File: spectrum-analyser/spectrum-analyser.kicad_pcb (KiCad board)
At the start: 2 copper layers, 50 x 95 mm, 41 parts, among them J1 Conn_Coaxial, J2 Conn_01x02, Q1 PMOS, Q2 PMOS, Q3 Q_PMOS_GSD, Q4 Q_NMOS_GSD, Q5 Q_NMOS_GSD, SW1 SW_SPDT, SW2 SW_UP, SW3 SW_RIGHT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

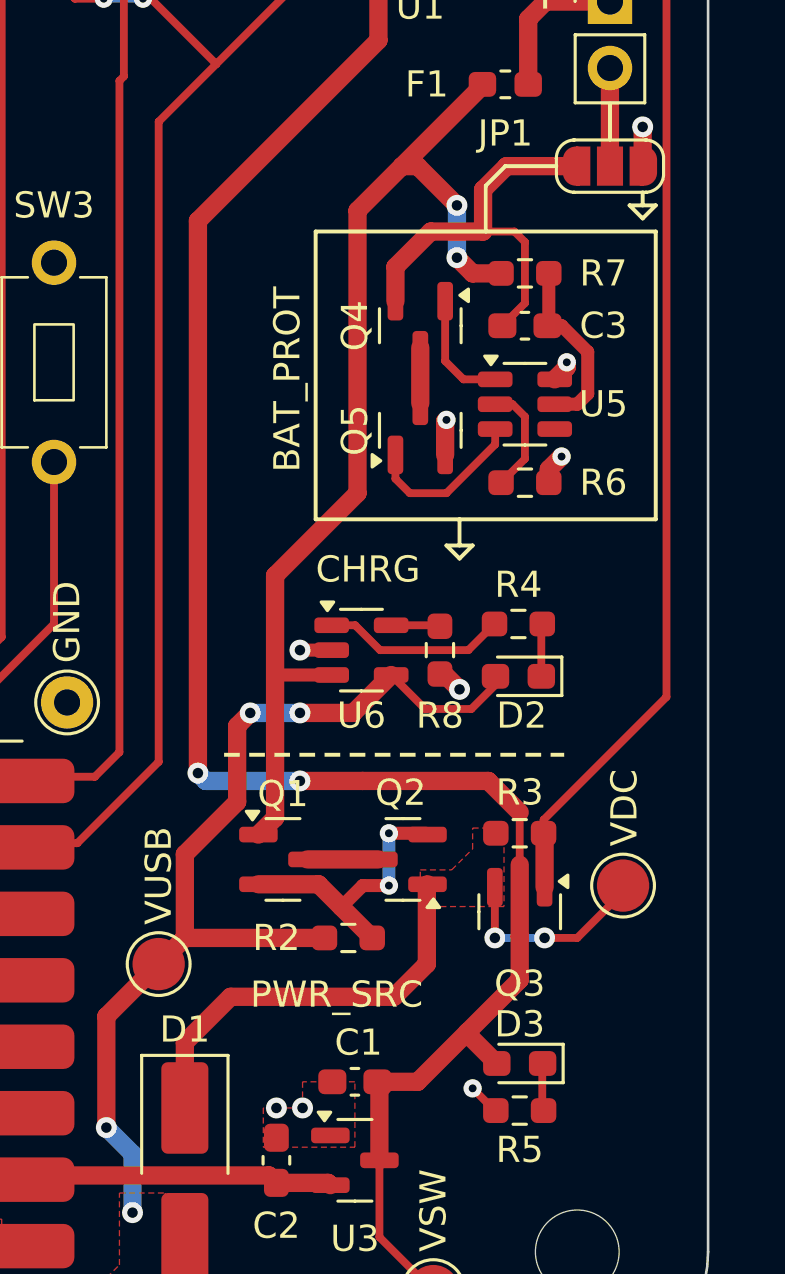
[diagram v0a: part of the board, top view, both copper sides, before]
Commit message: Assign component values and add charger capacitors
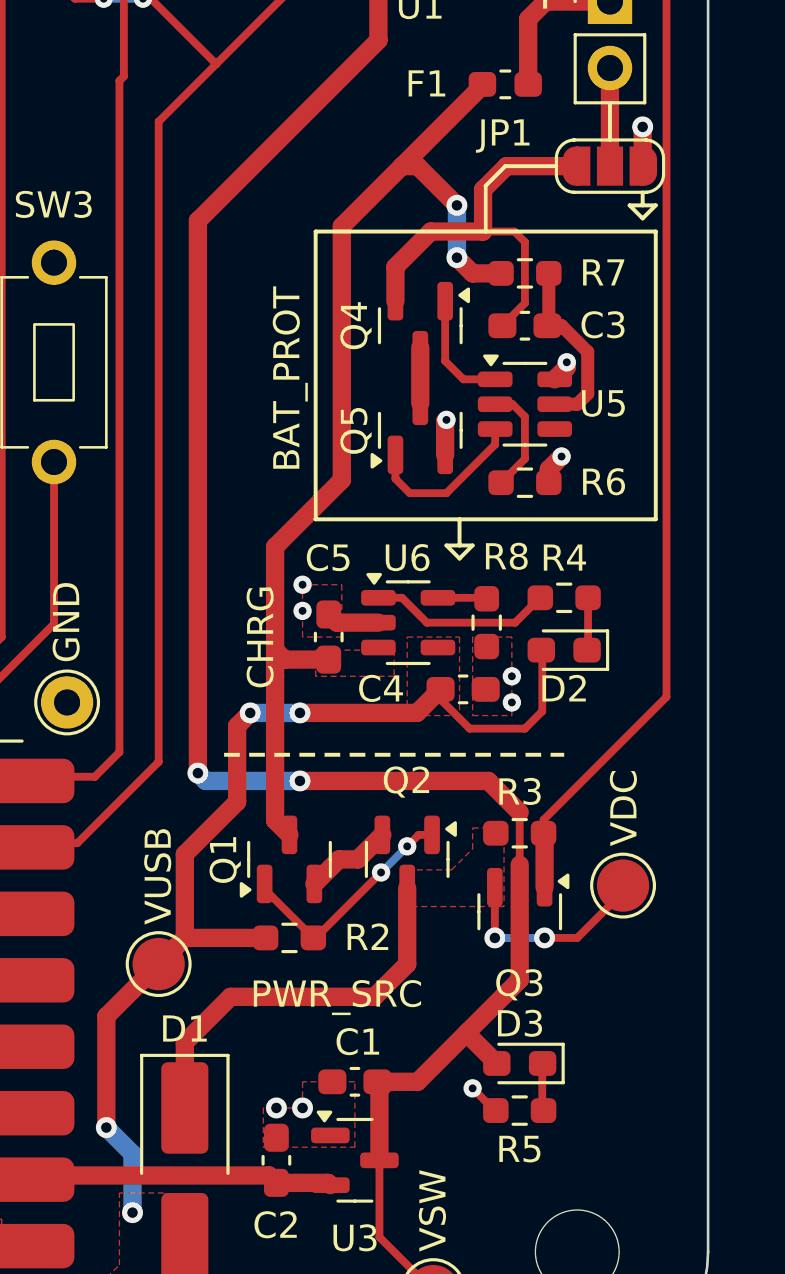
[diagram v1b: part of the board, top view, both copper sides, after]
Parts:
- added C4: 4u7, Capacitor_SMD:C_0603_1608Metric_Pad1.08x0.95mm_HandSolder, F.Cu at (135.6, 128.5)
- added C5: 4u7, Capacitor_SMD:C_0603_1608Metric_Pad1.08x0.95mm_HandSolder, F.Cu at (130.5, 126.5)
- C1, C2: value C -> 1u
- F1: value Fuse -> 3A
- J1: value Conn_Coaxial -> SMA
- Q1, Q2: value PMOS -> Q_PMOS_GSD
- R1, R2: value R -> 10k
- R8: value 12k -> 10k
- moved R2 2.25 mm to (129.0, 138.0)
- moved R8 2.07 mm to (136.5, 126.0)
- moved U6 2.07 mm to (133.5, 126.0)
- moved D2 2.02 mm to (139.5, 127.0)
- moved R4 2.02 mm to (139.5, 125.0)
- moved Q1 0.25 mm to (129.0, 135.0), turned to 90 degrees
- moved Q2 0.16 mm to (133.5, 135.0), turned to -90 degrees
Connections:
- Q1 pad 1: +BATT -> /PWR_SRC_SW_G
- Q1 pad 2: /PWR_SRC_SW_G -> /PWR_SRC_SW_S
- Q1 pad 3: /PWR_SRC_SW_S -> +BATT
- Q2 pad 1: VDC -> /PWR_SRC_SW_G
- Q2 pad 2: /PWR_SRC_SW_G -> /PWR_SRC_SW_S
- Q2 pad 3: /PWR_SRC_SW_S -> VDC
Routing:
- net /PWR_SRC_SW_G: track 10.9 -> 9.00 mm
- net VUSB: track 38.4 -> 39.9 mm
- net VDC: track 23.6 -> 22.7 mm
- net /PWR_SRC_SW_S: track 2.71 -> 3.38 mm
- net GND: track 20.4 -> 20.2 mm, vias 12 -> 14
- added copper zone on F.Cu, net +BATT

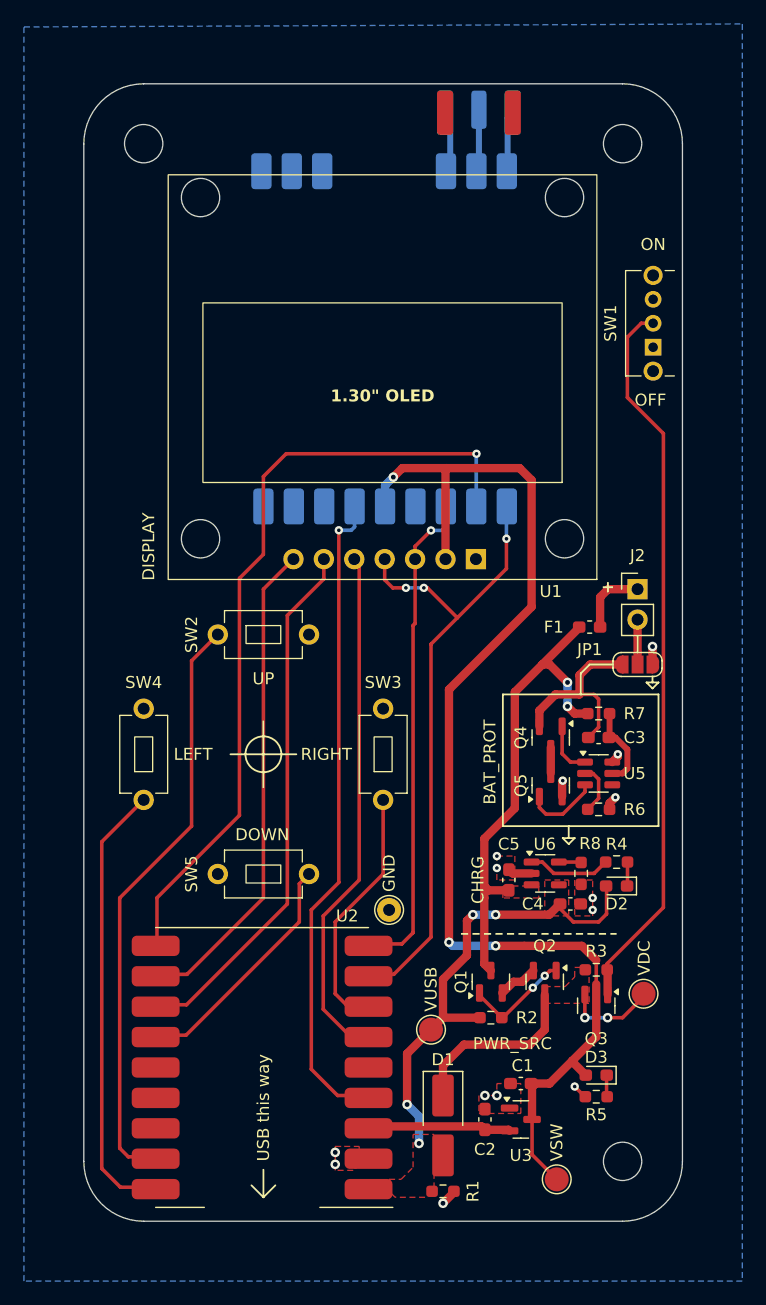
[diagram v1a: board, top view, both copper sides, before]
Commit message: Re-organise battery management sections
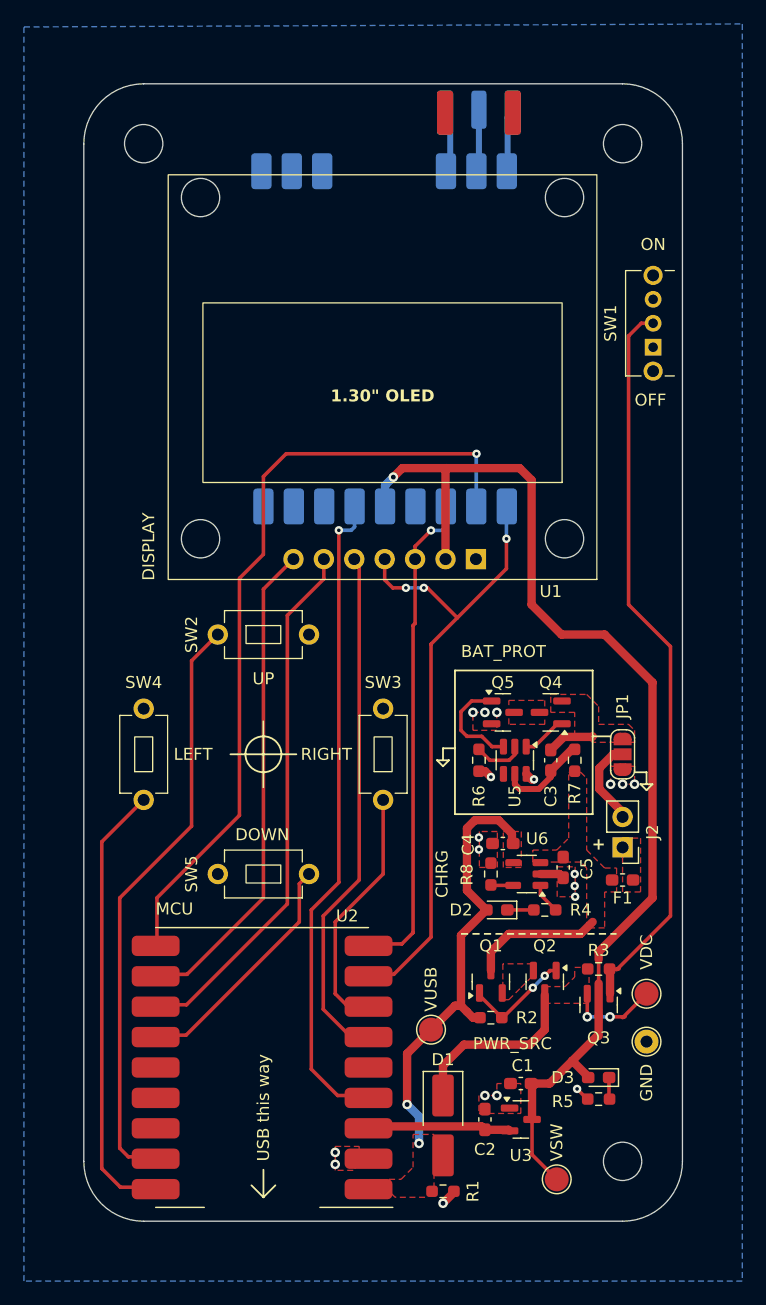
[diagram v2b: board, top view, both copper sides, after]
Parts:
- moved TP4 24.2 mm to (142.0, 140.0)
- moved J2 21.6 mm to (140.0, 123.8), turned to 180 degrees
- moved F1 21.3 mm to (140.0, 126.5)
- moved R6 10.8 mm to (128.0, 116.5), turned to -90 degrees
- moved D2 10.2 mm to (129.5, 129.0)
- moved JP1 7.60 mm to (140.0, 116.0), turned to -90 degrees
- moved C4 7.57 mm to (130.0, 123.5), turned to 180 degrees
- moved R8 7.54 mm to (129.0, 126.0), turned to -90 degrees
- moved Q5 7.29 mm to (130.0, 112.5), turned to 0 degrees
- moved R4 7.21 mm to (133.5, 129.0), turned to 180 degrees
- moved U5 7.09 mm to (131.0, 116.5), turned to -90 degrees
- moved C5 4.66 mm to (135.0, 125.5), turned to -90 degrees
- moved C3 4.43 mm to (134.0, 116.5), turned to -90 degrees
- moved R7 4.38 mm to (136.0, 116.5), turned to 90 degrees
- moved Q4 2.10 mm to (134.0, 112.5), turned to 180 degrees
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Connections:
- net Net-(Q4-D) renamed /Battery management/BAT_PROT_D
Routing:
- net +BATT: track 41.1 -> 11.1 mm, vias 2 -> 0
- net -BAT_PROT: track 16.1 -> 3.97 mm
- net +VSW: track 101.0 -> 95.0 mm, vias 3 -> 1
- net /Battery management/BAT_CONN_POS: track 5.90 -> 0.00 mm
- net CHRG_STAT: track 7.03 -> 2.63 mm
- net -BATT: track 3.75 -> 7.58 mm
- net /PWR_SRC_SW_S: track 3.38 -> 0.00 mm
- net GND: track 20.2 -> 17.3 mm, vias 14 -> 19
- net /Battery management/BAT_PROT_CO: track 6.31 -> 8.61 mm
- net /Battery management/BAT_PROT_D: track 2.12 -> 0.00 mm
- net VUSB: track 39.9 -> 38.1 mm, vias 4 -> 2
- net /PWR_SW: track 60.7 -> 61.6 mm
- net /Battery management/BAT_PROT_VDD: track 7.00 -> 7.79 mm
- net /Battery management/BAT_PROT_DO: track 4.49 -> 3.78 mm
- added copper zone on F.Cu, net -BAT_PROT
- added copper zone on F.Cu, net /Battery management/BAT_CONN_POS
- added copper zone on F.Cu, net /Battery management/BAT_PROT_D
- added copper zone on F.Cu, net /PWR_SRC_SW_S
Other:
- board text added: "MCU"

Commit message: Polish silkscreen and power switch layout
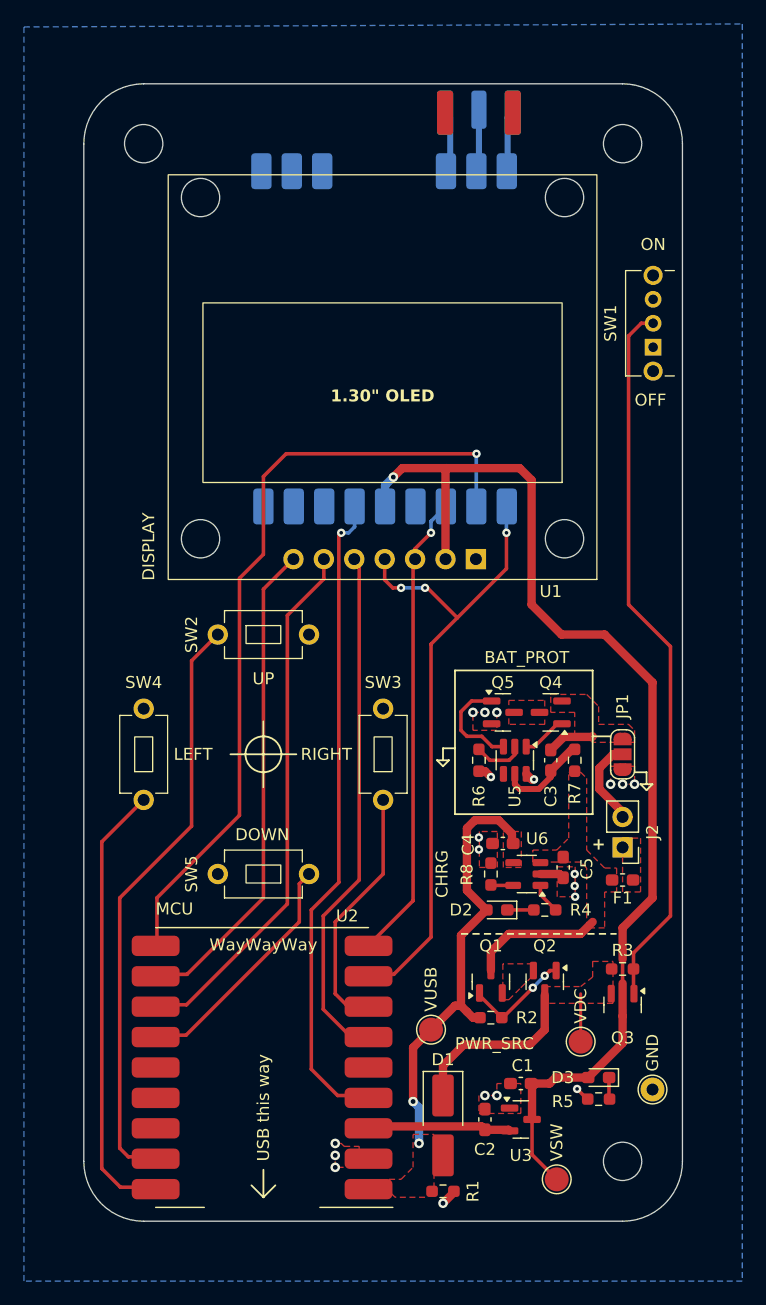
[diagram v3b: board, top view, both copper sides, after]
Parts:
- moved TP2 6.80 mm to (136.5, 140.0)
- moved TP4 4.03 mm to (142.5, 144.0)
- moved Q3 2.00 mm to (140.0, 136.9)
- moved R3 2.00 mm to (140.0, 133.9)
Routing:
- net VDC: track 22.7 -> 19.1 mm, vias 2 -> 0
- net SPI_CLK: track 41.3 -> 39.2 mm
- net /PWR_SW: track 61.6 -> 60.2 mm
- net GND: vias 19 -> 20
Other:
- board text added: "Spectrum analyser v1.0"
- board text added: "Thanassis Frank 20-11-24"
- board text added: "WayWayWay"

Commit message: Adjust button placement
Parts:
- moved SW2 1.00 mm to (110.0, 107.0)
- moved SW3 1.00 mm to (120.0, 117.0)
- moved SW4 1.00 mm to (100.0, 117.0)
- moved SW5 1.00 mm to (110.0, 127.0)
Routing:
- net GND: track 17.3 -> 25.4 mm
- net BTN_UP: track 49.7 -> 48.7 mm
- net BTN_RIGHT: track 21.1 -> 20.1 mm
- net BTN_LEFT: track 37.5 -> 36.5 mm
- net BTN_DOWN: track 20.1 -> 19.1 mm
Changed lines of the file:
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@@
 	(footprint "Thanassis_Foot:SW_PUSH_ADAFRUIT_SMALL"
 		(layer "F.Cu")
-		(at 110 126 180)
+		(at 110 127 180)
 		(property "Reference" "SW5"
 			(at 6 0 90)
@@
 	(footprint "Thanassis_Foot:SW_PUSH_ADAFRUIT_SMALL"
 		(layer "F.Cu")
-		(at 120 116 90)
+		(at 120 117 90)
 		(property "Reference" "SW3"
 			(at 6 0 0)
@@
 	(footprint "Thanassis_Foot:SW_PUSH_ADAFRUIT_SMALL"
 		(layer "F.Cu")
-		(at 100 116 90)
+		(at 100 117 90)
 		(property "Reference" "SW4"
 			(at 6 0 0)
@@
 		)
 		(fp_rect
-			(start -11.43 -13.97)
-			(end 11.43 12.7)
+			(start -11.43 -13.208)
+			(end 11.43 11.938)
 			(stroke
 				(width 0.05)
@@
 	(footprint "Thanassis_Foot:SW_PUSH_ADAFRUIT_SMALL"
 		(layer "F.Cu")
-		(at 110 106)
+		(at 110 107)
 		(property "Reference" "SW2"
 			(at -6 0 90)
@@
 	)
 	(gr_line
-		(start 110 113.25)
-		(end 110 118.75)
+		(start 110 114.25)
+		(end 110 119.75)
 		(stroke
 			(width 0.15)
@@
 	)
 	(gr_line
-		(start 107.25 116)
-		(end 112.75 116)
+		(start 107.25 117)
+		(end 112.75 117)
 		(stroke
 			(width 0.15)
@@
 	)
 	(gr_circle
-		(center 110 116)
-		(end 111.5 116)
+		(center 110 117)
+		(end 111.5 117)
 		(stroke
 			(width 0.15)
@@
 	)
 	(gr_circle
-		(center 110 116)
-		(end 100 116)
+		(center 110 117)
+		(end 100 117)
 		(stroke
 			(width 0.15)
@@
 	)
 	(gr_text "MCU"
-		(at 101 129.5 0)
+		(at 98 131 90)
 		(layer "F.SilkS" knockout)
 		(effects
@@
 				(thickness 0.15)
 			)
-			(justify left bottom)
+			(justify right bottom)
 		)
 	)
 	(gr_text "LEFT"
-		(at 102.5 116 0)
+		(at 102.5 117 0)
 		(layer "F.SilkS" knockout)
 		(effects
@@
 	)
 	(gr_text "WayWayWay"
-		(at 110 132.5 0)
+		(at 110 137 0)
 		(layer "F.SilkS")
 		(effects
@@
 	)
 	(gr_text "UP"
-		(at 110 109.1 0)
+		(at 110 110.1 0)
 		(layer "F.SilkS" knockout)
 		(effects
@@
 	)
 	(gr_text "DOWN"
-		(at 109.9 123.3 0)
+		(at 109.9 124.3 0)
 		(layer "F.SilkS" knockout)
 		(effects
@@
 	)
 	(gr_text "RIGHT"
-		(at 117.4 116 0)
+		(at 117.4 117 0)
 		(layer "F.SilkS" knockout)
 		(effects
@@
 		(layer "Dwgs.User")
 		(pts
-			(xy 110 116) (xy 120 116)
+			(xy 110 117) (xy 120 117)
 		)
 		(height 0)
 		(gr_text "10.0000 mm"
-			(at 115 114.85 0)
+			(at 115 115.85 0)
 			(layer "Dwgs.User")
 			(effects
@@
 	)
 	(segment
+		(start 125.25 71.25)
+		(end 125.5 71.5)
+		(width 0.5)
+		(layer "B.Cu")
+		(net 1)
+	)
+	(segment
 		(start 125.6 67.15)
 		(end 125.6 62.8375)
@@
 	)
 	(segment
+		(start 130.33 67.3)
+		(end 130.33 70.67)
+		(width 0.5)
+		(layer "B.Cu")
+		(net 1)
+	)
+	(segment
 		(start 125.25 67.5)
 		(end 125.6 67.15)
@@
 	)
 	(segment
+		(start 125.25 67.3)
+		(end 125.25 71.25)
+		(width 0.5)
+		(layer "B.Cu")
+		(net 1)
+	)
+	(segment
 		(start 125.6 62.8375)
 		(end 125.175 62.4125)
@@
 	)
 	(segment
+		(start 130.33 70.67)
+		(end 130 71)
+		(width 0.5)
+		(layer "B.Cu")
+		(net 1)
+	)
+	(segment
 		(start 140 135.13125)
 		(end 140 133.13125)
@@
 	)
 	(segment
-		(start 98 148.9)
-		(end 98.72 149.62)
+		(start 106.19 107)
+		(end 104 109.19)
 		(width 0.3)
 		(layer "F.Cu")
@@
 	)
 	(segment
-		(start 98.72 149.62)
-		(end 101.11 149.62)
+		(start 104 109.19)
+		(end 104 122)
 		(width 0.3)
 		(layer "F.Cu")
@@
 	)
 	(segment
-		(start 106.19 106)
-		(end 104 108.19)
+		(start 98 148.9)
+		(end 98.72 149.62)
 		(width 0.3)
 		(layer "F.Cu")
@@
 	)
 	(segment
-		(start 104 108.19)
-		(end 104 122)
+		(start 104 122)
+		(end 98 128)
 		(width 0.3)
 		(layer "F.Cu")
@@
 	)
 	(segment
-		(start 104 122)
-		(end 98 128)
+		(start 98.72 149.62)
+		(end 101.11 149.62)
 		(width 0.3)
 		(layer "F.Cu")
@@
 	)
 	(segment
-		(start 116 130)
-		(end 116 136)
+		(start 116 131.5)
+		(end 120 127.5)
 		(width 0.3)
 		(layer "F.Cu")
@@
 	)
 	(segment
-		(start 116.92 136.92)
-		(end 118.89 136.92)
+		(start 120 127.5)
+		(end 120 120.81)
 		(width 0.3)
 		(layer "F.Cu")
@@
 	)
 	(segment
-		(start 120 126)
-		(end 116 130)
+		(start 116.92 136.92)
+		(end 116 136)
 		(width 0.3)
 		(layer "F.Cu")
@@
 	)
 	(segment
-		(start 116 136)
+		(start 118.89 136.92)
 		(end 116.92 136.92)
 		(width 0.3)
@@
 	)
 	(segment
-		(start 120 119.81)
-		(end 120 126)
+		(start 116 136)
+		(end 116 131.5)
 		(width 0.3)
 		(layer "F.Cu")
@@
 	)
 	(segment
-		(start 96.5 123.31)
-		(end 96.5 150.6)
-		(width 0.3)
-		(layer "F.Cu")
-		(net 19)
-	)
-	(segment
-		(start 100 119.81)
-		(end 96.5 123.31)
+		(start 98.06 152.16)
+		(end 101.11 152.16)
 		(width 0.3)
 		(layer "F.Cu")
@@
 	)
 	(segment
-		(start 98.06 152.16)
-		(end 101.11 152.16)
+		(start 100 120.81)
+		(end 96.5 124.31)
 		(width 0.3)
 		(layer "F.Cu")
@@
 	)
 	(segment
-		(start 113 130)
-		(end 113 126.81)
+		(start 96.5 124.31)
+		(end 96.5 150.6)
 		(width 0.3)
 		(layer "F.Cu")
-		(net 20)
+		(net 19)
 	)
 	(segment
-		(start 113 126.81)
-		(end 113.81 126)
+		(start 113.81 129.19)
+		(end 113.81 127)
 		(width 0.3)
 		(layer "F.Cu")
@@
 	(segment
 		(start 103.54 139.46)
-		(end 113 130)
+		(end 113.81 129.19)
 		(width 0.3)
 		(layer "F.Cu")
@@
 	(segment
 		(start 118 100.11)
-		(end 118 126.5)
+		(end 118 128)
 		(width 0.3)
 		(layer "F.Cu")
@@
 	)
 	(segment
-		(start 118 126.5)
-		(end 115 129.5)
+		(start 118 128)
+		(end 115 131)
 		(width 0.3)
 		(layer "F.Cu")
@@
 	)
 	(segment
-		(start 115 129.5)
+		(start 115 131)
 		(end 115 137.3)
 		(width 0.3)
@@
 	)
 	(segment
-		(start 117.16 139.46)
-		(end 118.89 139.46)
+		(start 115 137.3)
+		(end 117.16 139.46)
 		(width 0.3)
 		(layer "F.Cu")
@@
 	)
 	(segment
-		(start 115 137.3)
-		(end 117.16 139.46)
+		(start 117.16 139.46)
+		(end 118.89 139.46)
 		(width 0.3)
 		(layer "F.Cu")
@@
 	)
 	(segment
-		(start 114 129)
-		(end 116.3 126.7)
+		(start 118.89 144.54)
+		(end 118.85 144.5)
 		(width 0.3)
 		(layer "F.Cu")
@@
 	)
 	(segment
-		(start 116.3 126.7)
+		(start 116.3 128.2)
 		(end 116.3 97.7)
 		(width 0.3)
@@
 	)
 	(segment
-		(start 118.89 144.54)
-		(end 118.85 144.5)
+		(start 116.2 144.5)
+		(end 114 142.3)
 		(width 0.3)
 		(layer "F.Cu")
@@
 	)
 	(segment
-		(start 114 142.3)
-		(end 114 129)
+		(start 118.85 144.5)
+		(end 116.2 144.5)
 		(width 0.3)
 		(layer "F.Cu")
@@
 	)
 	(segment
-		(start 118.85 144.5)
-		(end 116.2 144.5)
+		(start 114 142.3)
+		(end 114 130.5)
 		(width 0.3)
 		(layer "F.Cu")
@@
 	)
 	(segment
-		(start 116.3 97.7)
-		(end 116.5 97.5)
+		(start 114 130.5)
+		(end 116.3 128.2)
 		(width 0.3)
 		(layer "F.Cu")
@@
 	)
 	(segment
-		(start 116.2 144.5)
-		(end 114 142.3)
+		(start 116.3 97.7)
+		(end 116.5 97.5)
 		(width 0.3)
 		(layer "F.Cu")
@@
 		)
 	)
+	(group ""
+		(members "04865d97-58f2-4a60-991e-46410c0538b9" "13b44e8e-6f56-4d7c-8307-a494baa2bdd9"
+			"227b7279-7126-4646-9b99-706488caac09" "22fc4f9c-d860-4384-b974-8bc223e24f96"
+			"4535081e-e11f-4761-850f-7903acc659cb" "5b99e26e-ad99-467f-8780-ce0069d58f05"
+			"a5b72dc5-89f6-431e-9c07-470e3496b220" "dddd2707-1a4a-4d7f-b926-2c0bbfef476e"
+			"e4ca9767-5d75-4081-b99e-4659b2e3e33a" "f666f3db-846f-468d-b846-6514294ef4d8"
+			"f886bd49-2d75-4c44-b76b-7225c8da0231" "fcab85ef-a3bc-41bd-81df-3a9f75884311"
+		)
+	)
+	(group ""
+		(members "0dc3ab5e-24b9-4123-8565-17fddb471c60" "637fd413-9dc1-4e82-ab36-cb2cfedb9f1d")
+	)
 )

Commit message: Add Batt+ test point
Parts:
- added TP4: TestPoint, TestPoint:TestPoint_Pad_D2.0mm, F.Cu at (137.5, 131.0)
- moved R1 14.5 mm to (125.0, 138.0), turned to 0 degrees
- moved TP1 3.50 mm to (124.0, 135.5)
- moved D1 1.50 mm to (125.0, 148.5)
- moved C3 1.00 mm to (134.0, 115.5)
- moved C4 1.00 mm to (130.0, 122.5)
- moved C5 1.00 mm to (135.0, 124.5)
- moved D2 1.00 mm to (129.5, 128.0)
- moved F1 1.00 mm to (140.0, 125.5)
- moved J2 1.00 mm to (140.0, 122.8)
- moved JP1 1.00 mm to (140.0, 115.0)
- moved Q4 1.00 mm to (134.0, 111.5)
- moved Q5 1.00 mm to (130.0, 111.5)
- moved R4 1.00 mm to (133.5, 128.0)
- moved R6 1.00 mm to (128.0, 115.5)
- moved R7 1.00 mm to (136.0, 115.5)
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- renumbered TP4 to TP5
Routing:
- net VUSB: track 37.7 -> 42.1 mm
- net +3V3: track 11.8 -> 12.8 mm
- net /PWR_SRC_SW_G: vias 2 -> 0
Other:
- board text added: "BATT+"
- board text added: "Thanassis Frank 11/24"
- board text removed: "Thanassis Frank 20-11-24"
